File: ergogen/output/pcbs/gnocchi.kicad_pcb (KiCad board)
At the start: 2 copper layers, 45 parts

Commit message: Fix up kicad pcb
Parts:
- added REF**: Encoder_Panasonic_EVQWGD001, RollerEncoder_Panasonic_EVQWGD001, F.Cu at (135.0, 116.0)
- added S45: , ceoloide:switch_mx, B.Cu at (246.8, 148.1)
- moved S23 253.5 mm to (135.0, 116.0)
- moved S40 70.5 mm to (293.0, 54.3), turned to 0 degrees
- moved S34 47.8 mm to (331.0, 45.7)
- moved S37 45.1 mm to (312.0, 51.4)
- moved S31 38.4 mm to (350.0, 50.5)
- moved S44 30.4 mm to (251.7, 118.1), turned to 35 degrees
- moved S42 30.4 mm to (275.0, 106.0), turned to 20 degrees
- moved S25 29.7 mm to (388.0, 81.0)
- moved S28 29.7 mm to (369.0, 65.7)
- moved S24 19.0 mm to (388.0, 100.0)
- moved S26 19.0 mm to (369.0, 103.8)
- moved S27 19.0 mm to (369.0, 84.8)
- moved S29 19.0 mm to (350.0, 88.6)
- moved S30 19.0 mm to (350.0, 69.5)
- moved S32 19.0 mm to (331.0, 83.8)
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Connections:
- S23 pad 2: mirror_matrix_xtra_pinky_bottom -> hardware_stick_pos
- S24 pad 2: mirror_matrix_xtra_pinky_home -> mirror_matrix_xtra_pinky_bottom
- S25 pad 2: mirror_matrix_pinky_bottom -> mirror_matrix_xtra_pinky_home
- S26 pad 2: mirror_matrix_pinky_home -> mirror_matrix_pinky_bottom
- S27 pad 2: mirror_matrix_pinky_top -> mirror_matrix_pinky_home
- S28 pad 2: mirror_matrix_ring_bottom -> mirror_matrix_pinky_top
- S29 pad 2: mirror_matrix_ring_home -> mirror_matrix_ring_bottom
- S30 pad 2: mirror_matrix_ring_top -> mirror_matrix_ring_home
- S31 pad 2: mirror_matrix_middle_bottom -> mirror_matrix_ring_top
- S32 pad 2: mirror_matrix_middle_home -> mirror_matrix_middle_bottom
- S33 pad 2: mirror_matrix_middle_top -> mirror_matrix_middle_home
- S34 pad 2: mirror_matrix_index_bottom -> mirror_matrix_middle_top
- S35 pad 2: mirror_matrix_index_home -> mirror_matrix_index_bottom
- S36 pad 2: mirror_matrix_index_top -> mirror_matrix_index_home
- S37 pad 2: mirror_matrix_inner_bottom -> mirror_matrix_index_top
- S38 pad 2: mirror_matrix_inner_home -> mirror_matrix_inner_bottom
- S39 pad 2: mirror_matrix_inner_top -> mirror_matrix_inner_home
- S40 pad 2: mirror_thumb_tucky_top -> mirror_matrix_inner_top
- S41 pad 2: mirror_thumb_tucky_bottom -> mirror_thumb_tucky_top
- S42 pad 2: mirror_thumb_middle_top -> mirror_thumb_tucky_bottom
- S43 pad 2: mirror_thumb_middle_bottom -> mirror_thumb_middle_top
- S44 pad 2: mirror_thumb_reachy_top -> mirror_thumb_middle_bottom
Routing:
- net hardware_stick_pos: track 0.00 -> 23.1 mm, vias 0 -> 1
- net GND: track 465.7 -> 476.2 mm, vias 44 -> 45
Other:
- board outline added: 2.4 x 14.6 mm

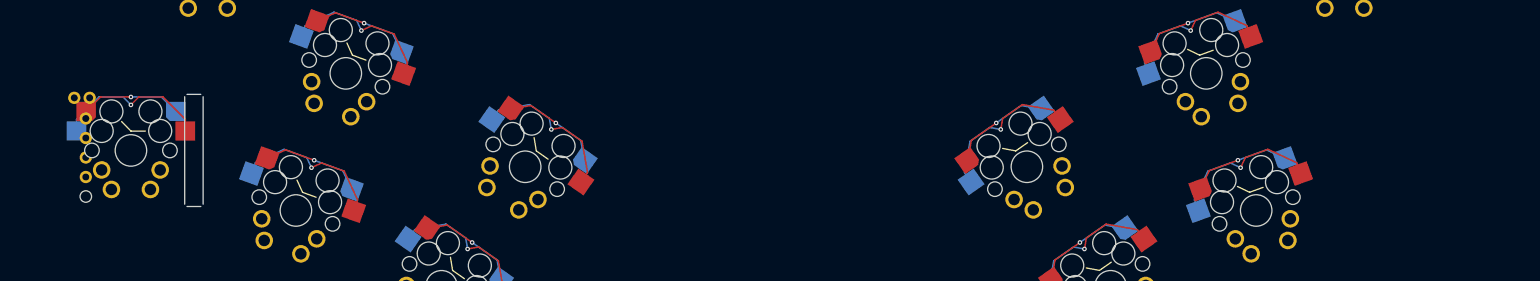
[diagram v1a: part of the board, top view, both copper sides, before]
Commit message: Make wheel work (need to find a better way to map keys)
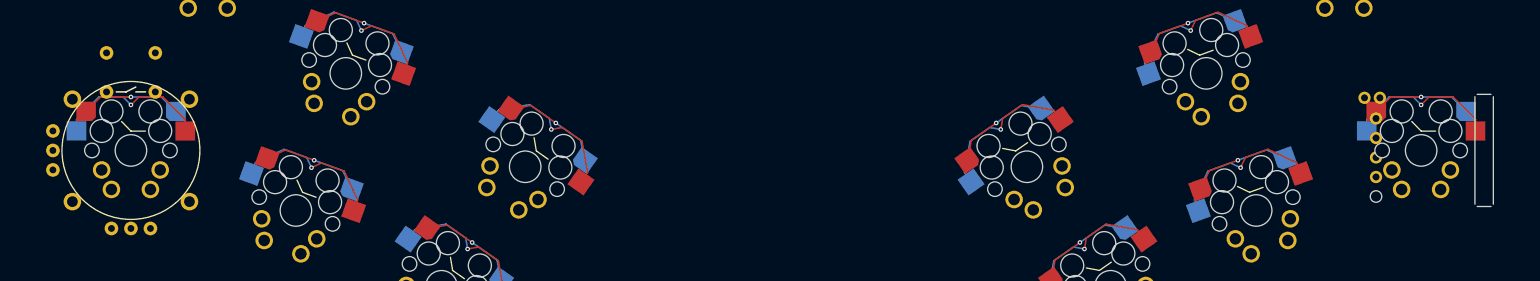
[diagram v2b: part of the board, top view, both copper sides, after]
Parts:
- added J1: , JOYSTICK, F.Cu at (135.0, 116.0)
- added S46: , ceoloide:switch_mx, B.Cu at (303.0, 116.0)
- moved REF** 168.0 mm to (303.0, 116.0)
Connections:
- net hardware_stick_pos renamed hardware
- net stick_pos_default renamed mirror_default_default
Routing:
- net mirror_hardware: track 0.00 -> 23.1 mm, vias 0 -> 1
- net GND: track 476.2 -> 486.8 mm, vias 45 -> 46
